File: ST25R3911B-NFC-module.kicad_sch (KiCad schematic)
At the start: 46 parts, among them J1 USB_C_Receptacle_USB2.0_16P, SW2 SW_Push, SW3 SW_Push, U1 ST25R3911B-AQF, U2 AP1117-33, U3 W25Q128JVS, U4 RP2040, Y1 Crystal_GND24

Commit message: схему вроде сделал, надо только понять как вообще адекватно, а главное симметрично мне провести к антенне всё что надобно
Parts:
- added C1, C26, C27, C31, C39, C43, C45: 100nF, Capacitor_SMD:C_0402_1005Metric, symbol Device:C
- added C16, C17: 8pF, Capacitor_SMD:C_0402_1005Metric, symbol Device:C
- added C18, C22: 5.6pF, Capacitor_SMD:C_0402_1005Metric, symbol Device:C
- added C19, C23: 12pF, Capacitor_SMD:C_0402_1005Metric, symbol Device:C
- added C20, C24: 27pF, Capacitor_SMD:C_0402_1005Metric, symbol Device:C
- added C21, C25: 56pF, Capacitor_SMD:C_0402_1005Metric, symbol Device:C
- added C28: 10uF, Capacitor_SMD:C_0402_1005Metric, symbol Device:C
- added C38, C42, C44, C46: 22uF, Capacitor_SMD:C_0402_1005Metric, symbol Device:C
- added L1: LQG18HN2N7S00D, Inductor_SMD:L_0603_1608Metric, symbol Device:L
- added R1: CRF0805-FZ-R010ELF, PCM_Resistor_SMD_AKL:R_0805_2012Metric_Pad1.15x1.40mm, symbol Device:R
- added R11: CRF0805-FZ-R010ELF, PCM_Resistor_SMD_AKL:R_0805_2012Metric, symbol Device:R
- added R12, R2: 1K, PCM_Resistor_SMD_AKL:R_0402_1005Metric, symbol Device:R
- added R13, R7: 100K, PCM_Resistor_SMD_AKL:R_0402_1005Metric, symbol Device:R
- added R14, R15, R16, R17, R18, R19: 0R, PCM_Resistor_SMD_AKL:R_0402_1005Metric, symbol Device:R
- added TP3, TP4: ~, TestPoint:TestPoint_Pad_1.5x1.5mm, symbol Connector:TestPoint
- added TP5: CSI, TestPoint:TestPoint_Pad_D1.0mm, symbol Connector:TestPoint
- added TP6: CSO, TestPoint:TestPoint_Pad_D1.0mm, symbol Connector:TestPoint
- added U3: LM358D, PCM_Package_SO_AKL:SO-8_3.9x4.9mm_P1.27mm, symbol PCM_Amplifier_Operational_AKL:LM358D
- added Y2: WTL2M85589FO, Crystal:Crystal_SMD_2520-4Pin_2.5x2.0mm, symbol Device:Crystal_GND24
- renumbered C17 to C10, C18 to C11, C19 to C12, C20 to C13, C21 to C14, C22 to C15, C1 to C2, C23 to C29, C10 to C3, C24 to C30, C30 to C32, C29 to C33, C25 to C34, C26 to C35, C32 to C36, C31 to C37, C27 to C40, C28 to C41, C15 to C5, C5 to C6, C6 to C7, C7 to C8, C16 to C9, L1 to L2, L2 to L3, R9 to R10, R10 to R20, R11 to R21, R1 to R3, R2 to R4, R7 to R8, R8 to R9, SW2 to SW1, SW3 to SW2, TP3 to TP1, TP4 to TP2, U2 to U1, U3 to U2, U1 to U5
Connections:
- net +3.3V: now also U5.1 (VDD_IO), C1.1, C26.1, R11.2, R12.2, U3.8 (V+); no longer C4.1, C6.1, C7.1, U1.2 (VO)
- net +5V USB: now also R1.1, TP3.1, U3.3 (+)
- net Earth: now also U5.12 (VSN_RF), U5.21 (VSS), U5.26 (VSN_A), U5.33 (EP), U5.6 (VSN_D), C1.2, C16.1, C17.2, C26.2, C27.2, C28.2, C31.2, C38.2, C39.2, C42.2, C43.2, C44.2, C45.2, C46.2, TP4.1, U3.4 (V-), Y2.2, Y2.4
- net RFI1: now also U5.22 (RFI1)
- net RFI2: now also U5.23 (RFI2)
- net RFO1: now also U5.10 (RFO1)
- net RFO2: now also U5.11 (RFO2)
- net TRIM2: now reaches C35.2, C36.2, C41.1, R21.2
- net TRIM2: now also C22.2, C23.2, C24.2, C25.2
- net TRIM1: now reaches C33.2, C34.2, C40.1, R20.2
- net TRIM1: now also C18.2, C19.2, C20.2, C21.2
- net SCLK: now reaches U4.16 (GPIO13)
- net SCLK: now also R16.2
- net !SS: now reaches U4.17 (GPIO14)
- net !SS: now also R17.2
- net MOSI: now reaches U4.18 (GPIO15)
- net MOSI: now also R15.2
- net MISO: now reaches U4.27 (GPIO16)
- net MISO: now also R14.2
- net MCU_CLK: now reaches U4.32 (GPIO21)
- net MCU_CLK: now also R19.2
- net IRQ: now reaches U4.34 (GPIO22)
- net IRQ: now also R18.2
- net at R20.1: now also ANT1.2; no longer ANT1.1
- net at R21.1: now also ANT1.1; no longer ANT1.2
- net TRIM1_3: now reaches U5.13 (TRIM1_3)
- net TRIM1_3: now also C21.1
- net TRIM2_3: now reaches U5.14 (TRIM2_3)
- net TRIM2_3: now also C25.1
- net TRIM1_2: now reaches U5.15 (TRIM1_2)
- net TRIM1_2: now also C20.1
- net TRIM2_2: now reaches U5.16 (TRIM2_2)
- net TRIM2_2: now also C24.1
- net TRIM1_1: now reaches U5.17 (TRIM1_1)
- net TRIM1_1: now also C19.1
- net TRIM2_1: now reaches U5.18 (TRIM2_1)
- net TRIM2_1: now also C23.1
- net TRIM1_0: now reaches U5.19 (TRIM1_0)
- net TRIM1_0: now also C18.1
- net at U5.2 (CSO): now also TP6.1
- net TRIM2_0: now reaches U5.20 (TRIM2_0)
- net TRIM2_0: now also C22.1
- net at U5.24 (AGD): now also C31.1, C38.1
- net at U5.25 (CSI): now also TP5.1
- net at U5.27 (IRQ): now also R18.1
- net at U5.28 (MCU_CLK): now also R19.1
- net at U5.29 (MISO): now also R14.1
- net at U5.3 (VSP_D): now also C45.1, C46.1
- net at U5.30 (MOSI): now also R15.1
- net at U5.31 (SCLK): now also R16.1
- net at U5.32 (/SS): now also R17.1
- net at U5.4 (XTO): now also C16.2, Y2.3
- net at U5.5 (XTI): now also C17.1, Y2.1
- net at U5.7 (VSP_A): now also C43.1, C44.1
- net at U5.8 (VDD): now also C27.1, C28.1, L1.2
- net at U5.9 (VSP_RF): now also C39.1, C42.1
- net +5V renamed +5V DOMAIN
- net +5V DOMAIN: now also L1.1, R1.2, R2.2
- new net: R12.1, R13.2, U3.6 (-)
- new net: R2.1, R7.2, U3.2 (-)
- new net +3.3V_LDO: C4.1, C6.1, C7.1, R11.1, U1.2 (VO), U3.5 (+)
- new net CURRENT_3V3: R13.1, U3.7
- new net CURRENT_5V: R7.1, U3.1
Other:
- moved on the sheet: ANT1, C10, C11, C12, C13, C14, C15, C2, C29, C3, C30, C32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

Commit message: rev0 готова
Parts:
- added LED1, LED2, LED3: LED_0402, LED_SMD:LED_0402_1005Metric, symbol PCM_LED_AKL:LED_0402
- added R22, R23, R24: 200R, PCM_Resistor_SMD_AKL:R_0402_1005Metric, symbol Device:R
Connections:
- net Earth: now also LED1.1 (K), LED2.1 (K), LED3.1 (K)
- net at U4.12 (GPIO9): now also R24.1
- net at U4.13 (GPIO10): now also R23.1
- net at U4.14 (GPIO11): now also R22.1
- new net: LED3.2 (A), R24.2
- new net: LED2.2 (A), R23.2
- new net: LED1.2 (A), R22.2

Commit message: Добавлено примечание чтобы быстро разобраться если не заработает
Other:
- note added: "Нужны ли подтяжки на SPI? ( по линиям данных и клоку )"

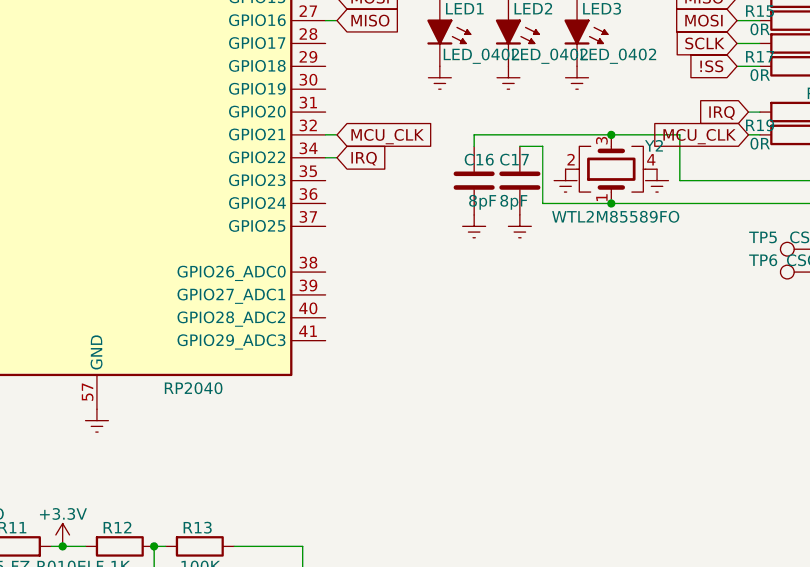
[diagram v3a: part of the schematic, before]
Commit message: Довёл соединения для АЦП чтения потребления тока для доменов питания
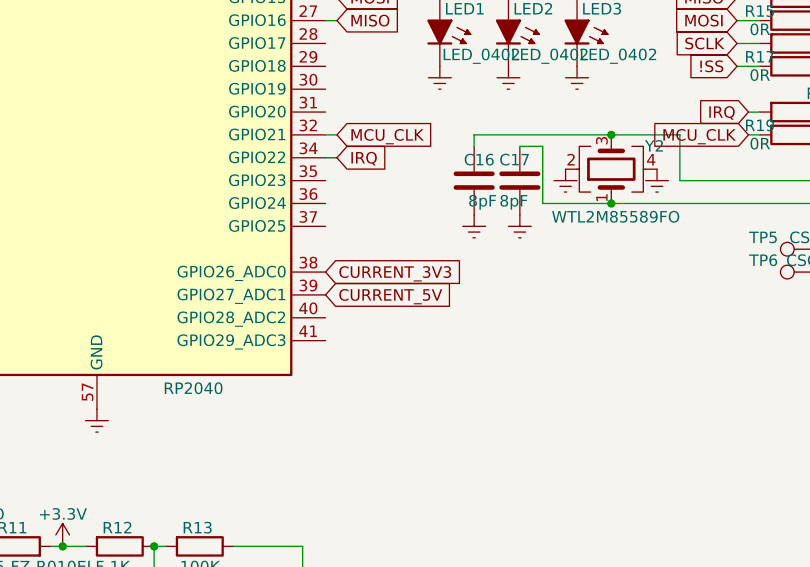
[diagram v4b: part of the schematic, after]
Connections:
- net CURRENT_3V3: now also U4.38 (GPIO26_ADC0)
- net CURRENT_5V: now also U4.39 (GPIO27_ADC1)
